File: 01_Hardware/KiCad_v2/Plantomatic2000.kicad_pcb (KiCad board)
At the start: 4 copper layers, 84 x 51 mm, 202 parts, among them J103 USB_C_Receptacle_USB2.0_16P, Q101 IRLL014NP, Q102 IRLL014NP, Q104 NVTA7002NT1G, Q105 RU1E002SPTCL, Q106 NVTA7002NT1G, Q107 NVTA7002NT1G, Q108 RU1E002SPTCL, Q109 NVTA7002NT1G, Q110 RU1E002SPTCL, Q111 DTC143Z, Q112 DTC143Z, Q113 CSD17313Q2, U101 XC6220B331MR, U102 nPM1300, U103 ESP32-WROOM-32E, U104 TPS61287, U105 USBLC6-2P6, U106 CP2102N-A02-GQFN24, U107 DS3231M, U108 AT24CS01-SSHM

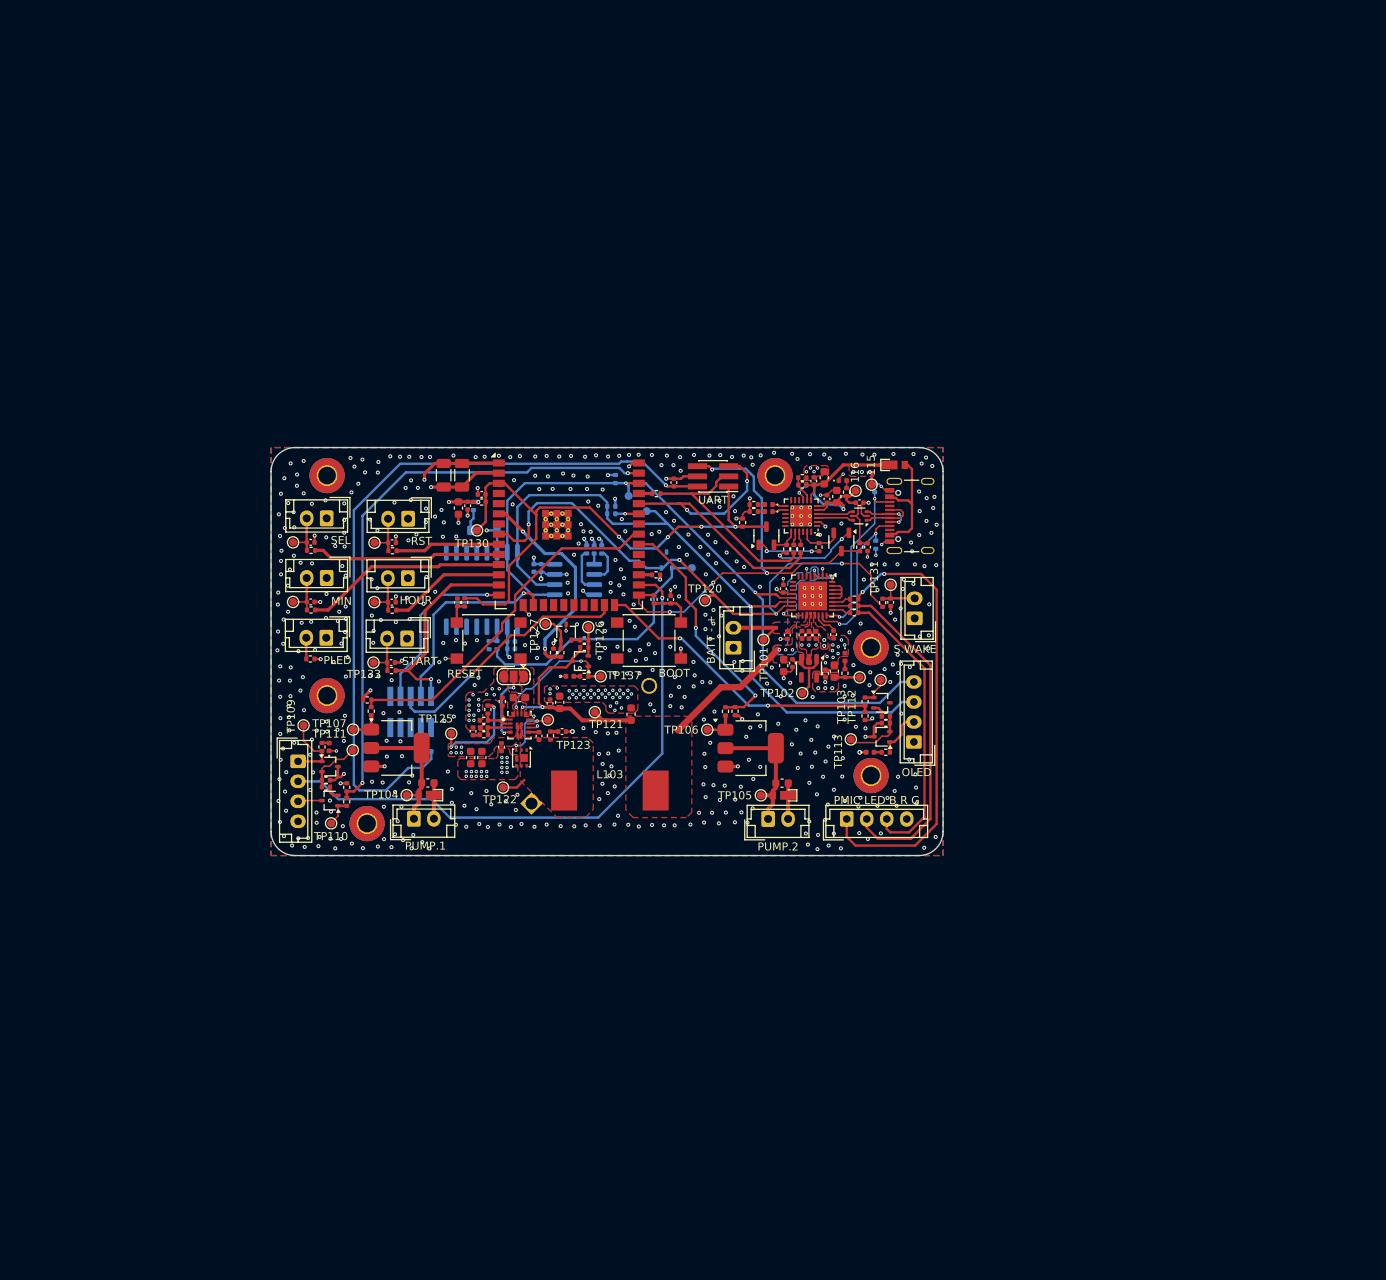
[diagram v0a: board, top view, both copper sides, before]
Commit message: Replaced BOOST converter, previous one didn't support +2A but rather 200 to 300mA, TO DO: re-do schematic annotation for BOOST, re-do BOM for BOOST
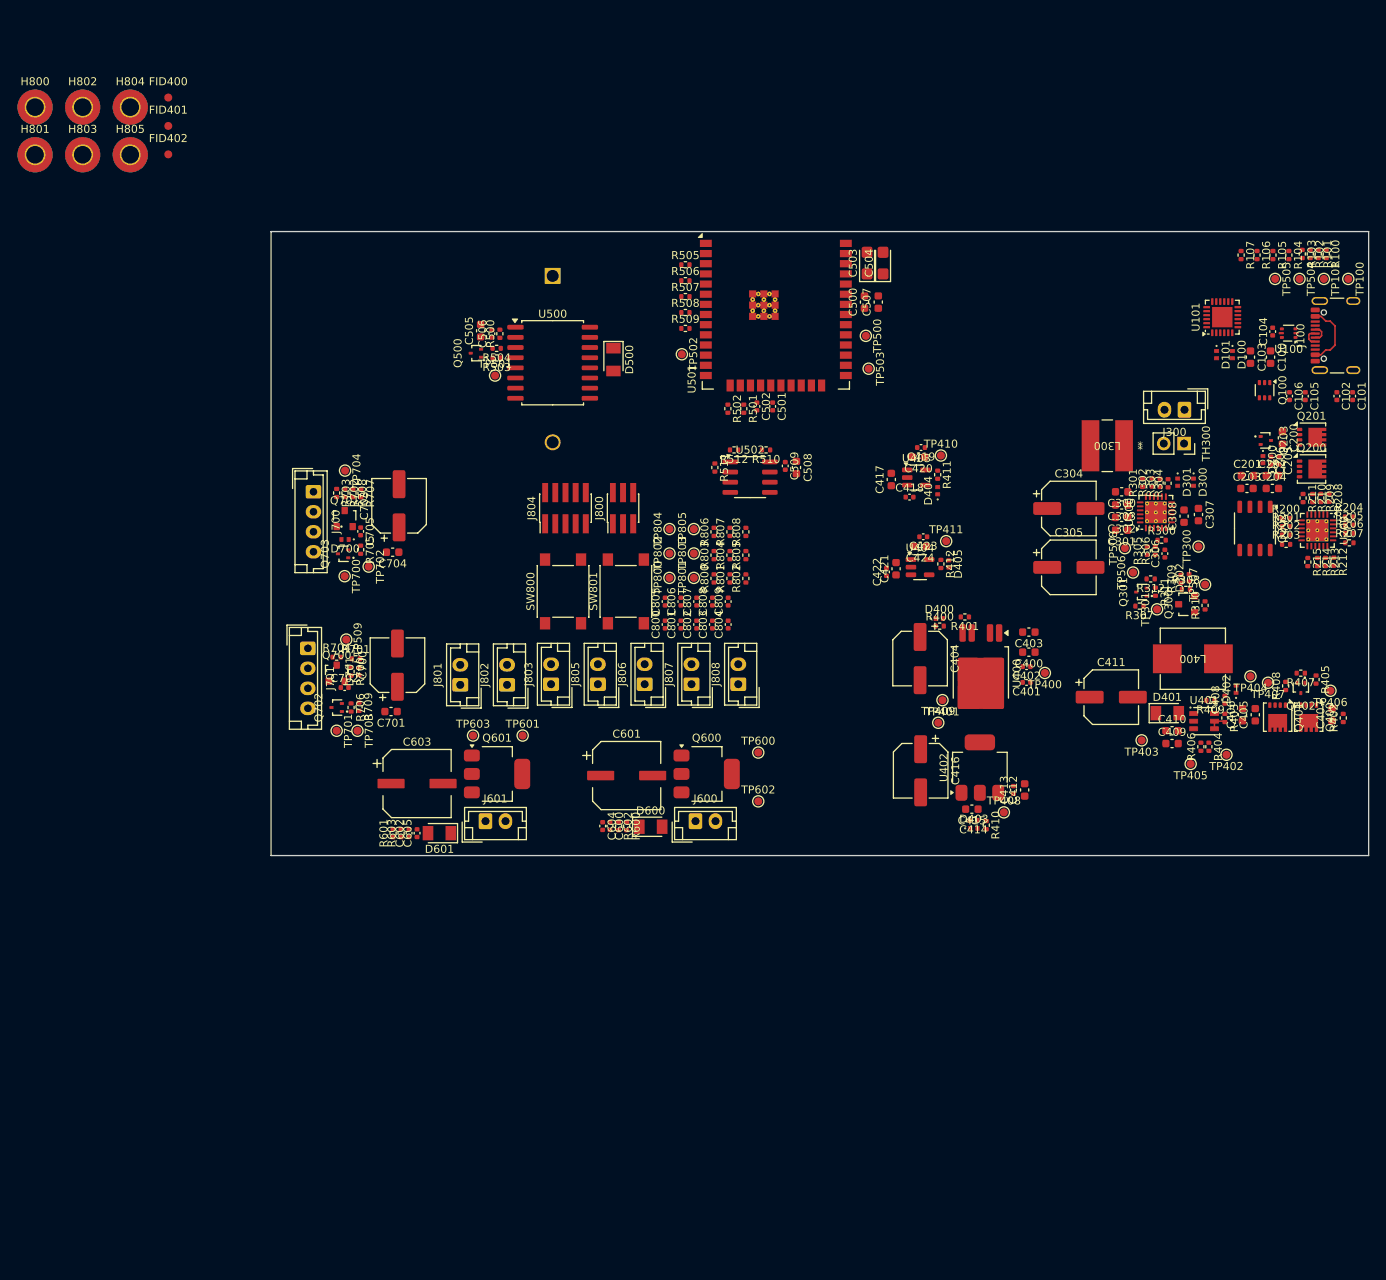
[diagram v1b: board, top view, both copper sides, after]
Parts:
- removed 115, 116, 132, 136, TP102, TP103, TP104, TP105, TP106, TP107, TP108, TP109, TP110, TP111, TP112, TP113, TP117, TP118, TP120, TP121, TP122, TP123, TP125, TP126, TP127, TP130, TP131, TP133, TP134, TP135, TP137: ~, TestPoint:TestPoint_Pad_D1.0mm
- removed BATT - +: Running LED, Connector_JST:JST_EH_B2B-EH-A_1x02_P2.50mm_Vertical
- removed BOOT, RESET: SW_Push, Button_Switch_SMD:SW_SPST_PTS645
- removed BT101: Battery_Cell, Battery:BatteryHolder_MYOUNG_BS-07-A1BJ001_CR2032
- removed C107, C108, C137, C144: 10uF, Capacitor_SMD:C_0402_1005Metric
- removed C109, C110, C123: 10uF, Capacitor_SMD:C_0603_1608Metric
- removed C111: 1uF, Capacitor_SMD:C_0402_1005Metric
- removed C112: 2.2uF, Capacitor_SMD:C_0402_1005Metric
- removed C113, C115, C116, C117, C118, C119, C122, C124, C129, C130, C132, C136, C138, C139, C140, C141, C142, C143, C145, C146, C147, C148: 100nF, Capacitor_SMD:C_0402_1005Metric
- removed C114, C133: 1uF, Capacitor_SMD:C_0603_1608Metric
- removed C120, C121: 47uF, Capacitor_SMD:C_0603_1608Metric
- removed C125: 58pF, Capacitor_SMD:C_0402_1005Metric
- removed C126, C135: 4.7nF, Capacitor_SMD:C_0402_1005Metric
- removed C127: 2.2uF, Capacitor_SMD:C_0603_1608Metric
- removed C128, C131: 4.7uF, Capacitor_SMD:C_0603_1608Metric
- removed C134: 22uF, Capacitor_SMD:C_0603_1608Metric
- removed D103, D104: SML-P13PTT86R, LED_SMD:LED_0402_1005Metric
- removed D106: 1N4148W, Diode_SMD:D_SOD-123
- removed D107, D111, D112, D113, D114: SML-P12U2TT86R, LED_SMD:LED_0402_1005Metric
- removed D108, D109, D110: SS14, Custom_Global_Footprints:SS14M_Flyback_Diode
- removed H101, H102, H103, H104, H105, H106: MountingHole_Pad, MountingHole:MountingHole_2.2mm_M2_Pad_TopBottom
- removed HOUR: Hour, Connector_JST:JST_EH_B2B-EH-A_1x02_P2.50mm_Vertical
- removed J103: USB_C_Receptacle_USB2.0_16P, Connector_USB:USB_C_Receptacle_Palconn_UTC16-G
- removed JTAG: Conn_02x05_Odd_Even, Connector_PinHeader_1.27mm:PinHeader_2x05_P1.27mm_Vertical_SMD
- removed L103: 4.7uH (SPM12565VT-4R7M-D), Custom_Global_Footprints:SPM12565VT-4R7M
- removed MIN: Minute, Connector_JST:JST_EH_B2B-EH-A_1x02_P2.50mm_Vertical
- removed OLED: JST_B4B, Connector_JST:JST_EH_B4B-EH-A_1x04_P2.50mm_Vertical
- removed PLED: Running LED, Connector_JST:JST_EH_B2B-EH-A_1x02_P2.50mm_Vertical
- removed PMIC LED B R G: JST_4B4, Connector_JST:JST_EH_B4B-EH-A_1x04_P2.50mm_Vertical
- removed PUMP.1, PUMP.2: JST_B2B, Connector_JST:JST_EH_B2B-EH-A_1x02_P2.50mm_Vertical
- removed Q101, Q102: IRLL014NP, Package_TO_SOT_SMD:SOT-223
- removed Q104, Q106, Q107, Q109: NVTA7002NT1G, Package_TO_SOT_SMD:SOT-323_SC-70
- removed Q105, Q108, Q110: RU1E002SPTCL, Package_TO_SOT_SMD:SOT-323_SC-70
- removed Q111, Q112: DTC143Z, Package_TO_SOT_SMD:SOT-23-3
- removed Q113: CSD17313Q2, Package_SON:Texas_DQK
- removed R108: 158K, Resistor_SMD:R_0402_1005Metric
- removed R109: 14K3, Resistor_SMD:R_0402_1005Metric
- removed R110, R121, R124, R126, R128, R129, R130, R132, R133, R140, R142, R143, R154: 10K, Resistor_SMD:R_0402_1005Metric
- removed R111: 40K, Resistor_SMD:R_0402_1005Metric
- removed R112, R119, R120, R123, R139, R148, R149, R150, R160, R161, R162, R163: 1K, Resistor_SMD:R_0402_1005Metric
- removed R113: 22K1, Resistor_SMD:R_0402_1005Metric
- removed R114, R115, R134, R135, R136, R137, R138, R146, R147, R164: 0R, Resistor_SMD:R_0402_1005Metric
- removed R116, R118, R159: 5K1, Resistor_SMD:R_0402_1005Metric
- removed R117: 47K5, Resistor_SMD:R_0402_1005Metric
- removed R122: 220R, Resistor_SMD:R_0402_1005Metric
- removed R125, R127, R131, R141, R156: 470R, Resistor_SMD:R_0402_1005Metric
- removed R144, R145, R151, R152, R153: 4K7, Resistor_SMD:R_0402_1005Metric
- removed R155, R157, R158: 12K, Resistor_SMD:R_0402_1005Metric
- removed RST: System Reset, Connector_JST:JST_EH_B2B-EH-A_1x02_P2.50mm_Vertical
- removed S.WAKE: System Wake Up, Connector_JST:JST_EH_B2B-EH-A_1x02_P2.50mm_Vertical
- removed SEL: ModSel, Jumper:SolderJumper-3_P1.3mm_Open_RoundedPad1.0x1.5mm
- removed SEL: Line Select, Connector_JST:JST_EH_B2B-EH-A_1x02_P2.50mm_Vertical
- removed START: Manual Start, Connector_JST:JST_EH_B2B-EH-A_1x02_P2.50mm_Vertical
- removed U102: nPM1300, Package_DFN_QFN:QFN-32-1EP_5x5mm_P0.5mm_EP3.6x3.6mm_ThermalVias
- removed U103: ESP32-WROOM-32E, RF_Module:ESP32-WROOM-32E
- removed U104: TPS61287, Custom_Global_Footprints:RZP0014A-MFG
- removed U105: USBLC6-2P6, Package_TO_SOT_SMD:SOT-666
- removed U106: CP2102N-A02-GQFN24, Package_DFN_QFN:QFN-24-1EP_4x4mm_P0.5mm_EP2.7x2.6mm_ThermalVias
- removed U107: DS3231M, Package_SO:SOIC-16W_7.5x10.3mm_P1.27mm
- removed U108: AT24CS01-SSHM, Package_SO:SOIC-8_3.9x4.9mm_P1.27mm
- removed UART: Conn_02x03_Odd_Even, Connector_PinHeader_1.27mm:PinHeader_2x03_P1.27mm_Vertical_SMD
- removed Water Sig: JST_4B4, Connector_JST:JST_EH_B4B-EH-A_1x04_P2.50mm_Vertical
- added BT500: BS-07-A1BJ001_CR2032, Battery:BatteryHolder_MYOUNG_BS-07-A1BJ001_CR2032, B.Cu at (149.8, 54.4)
- added C100: 4.7uF, Capacitor_SMD:C_0603_1608Metric, F.Cu at (239.5, 64.6)
- added C200: 4.7uF, Capacitor_SMD:C_0603_1608Metric, F.Cu at (241.0, 74.7)
- added C201: 1uF, Capacitor_SMD:C_0603_1608Metric, F.Cu at (236.7, 79.4)
- added C202: 1uF, Capacitor_SMD:C_0603_1608Metric, F.Cu at (239.8, 79.4)
- added C203: 1uF, Capacitor_SMD:C_0603_1608Metric, F.Cu at (236.6, 81.0)
- added C204: 1uF, Capacitor_SMD:C_0603_1608Metric, F.Cu at (239.8, 81.0)
- added C205: 100nF, Capacitor_SMD:C_0402_1005Metric, F.Cu at (240.6, 77.5)
- added C206: 100nF, Capacitor_SMD:C_0402_1005Metric, F.Cu at (239.6, 77.5)
- added C300: 1uF, Capacitor_SMD:C_0603_1608Metric, F.Cu at (220.9, 81.4)
- added C301: 10uF, Capacitor_SMD:C_0603_1608Metric, F.Cu at (220.9, 86.2)
- added C302: 10uF, Capacitor_SMD:C_0603_1608Metric, F.Cu at (220.9, 84.6)
- added C303: 10uF, Capacitor_SMD:C_0603_1608Metric, F.Cu at (220.9, 83.1)
- added C304: 47uF, Capacitor_SMD:CP_Elec_6.3x5.8, F.Cu at (214.3, 83.5)
- added C305: 47uF, Capacitor_SMD:CP_Elec_6.3x5.8, F.Cu at (214.3, 90.9)
- added C306: 47nF, Capacitor_SMD:C_0402_1005Metric, F.Cu at (226.3, 89.2)
- added C307: 10uF, Capacitor_SMD:C_0603_1608Metric, F.Cu at (230.5, 84.3)
- added C308: 4.7uF, Capacitor_SMD:C_0603_1608Metric, F.Cu at (228.7, 84.5)
- added C400: 10uF, Capacitor_SMD:C_0603_1608Metric, F.Cu at (209.3, 101.5)
- added C401: 100nF, Capacitor_SMD:C_0402_1005Metric, F.Cu at (209.0, 105.3)
- added C402: 100nF, Capacitor_SMD:C_0402_1005Metric, F.Cu at (209.0, 103.3)
- added C403: 10uF, Capacitor_SMD:C_0603_1608Metric, F.Cu at (209.3, 99.0)
- added C404: 47uF, Capacitor_SMD:CP_Elec_6.3x5.8, F.Cu at (195.7, 102.3)
- added C405: 1uF, Capacitor_SMD:C_0603_1608Metric, F.Cu at (237.6, 109.3)
- added C406: 1uF, Capacitor_SMD:C_0603_1608Metric, F.Cu at (236.0, 109.3)
- added C407: 1uF, Capacitor_SMD:C_0603_1608Metric, F.Cu at (247.2, 109.3)
- added C408: 100nF, Capacitor_SMD:C_0402_1005Metric, F.Cu at (233.8, 107.4)
- added C409: 1uF, Capacitor_SMD:C_0603_1608Metric, F.Cu at (227.2, 112.9)
- added C410: 10uF, Capacitor_SMD:C_0603_1608Metric, F.Cu at (227.2, 111.3)
- added C411: 47uF, Capacitor_SMD:CP_Elec_6.3x5.8, F.Cu at (219.6, 107.1)
- added C412: 10uF, Capacitor_SMD:C_0603_1608Metric, F.Cu at (208.8, 118.7)
- added C413: 100nF, Capacitor_SMD:C_0402_1005Metric, F.Cu at (207.4, 118.7)
- added C414: 100nF, Capacitor_SMD:C_0402_1005Metric, F.Cu at (202.4, 122.5)
- added C415: 10uF, Capacitor_SMD:C_0603_1608Metric, F.Cu at (202.2, 121.1)
- added C416: 47uF, Capacitor_SMD:CP_Elec_6.3x5.8, F.Cu at (195.8, 116.3)
- added C417: 10uF, Capacitor_SMD:C_0603_1608Metric, F.Cu at (192.1, 79.9)
- added C418: 100nF, Capacitor_SMD:C_0402_1005Metric, F.Cu at (194.4, 82.1)
- added C419: 100nF, Capacitor_SMD:C_0402_1005Metric, F.Cu at (195.8, 75.9)
- added C420: 10uF, Capacitor_SMD:C_0603_1608Metric, F.Cu at (195.5, 77.1)
- added C421: 10uF, Capacitor_SMD:C_0603_1608Metric, F.Cu at (192.7, 91.0)
- added C422: 100nF, Capacitor_SMD:C_0402_1005Metric, F.Cu at (191.5, 91.5)
- added C423: 100nF, Capacitor_SMD:C_0402_1005Metric, F.Cu at (196.1, 87.0)
- added C424: 10uF, Capacitor_SMD:C_0603_1608Metric, F.Cu at (195.7, 88.2)
- added C500: 22uF, Capacitor_SMD:C_0603_1608Metric, F.Cu at (188.8, 57.7)
- added C501: 100nF, Capacitor_SMD:C_0402_1005Metric, F.Cu at (177.3, 70.8)
- added C502: 100nF, Capacitor_SMD:C_0402_1005Metric, F.Cu at (175.3, 70.8)
- added C503: 10uF, Capacitor_Tantalum_SMD:CP_EIA-3216-18_Kemet-A, F.Cu at (189.1, 52.8)
- added C504: 10uF, Capacitor_Tantalum_SMD:CP_EIA-3216-18_Kemet-A, F.Cu at (191.1, 52.8)
- added C505: 10uF, Capacitor_SMD:C_0603_1608Metric, F.Cu at (140.8, 61.3)
- added C506: 100nF, Capacitor_SMD:C_0402_1005Metric, F.Cu at (142.2, 61.7)
- added C507: 1uF, Capacitor_SMD:C_0603_1608Metric, F.Cu at (190.5, 57.7)
- added C508: 10uF, Capacitor_SMD:C_0603_1608Metric, F.Cu at (180.3, 78.4)
- added C509: 100nF, Capacitor_SMD:C_0402_1005Metric, F.Cu at (178.9, 78.2)
- added C600: 100nF, Capacitor_SMD:C_0402_1005Metric, F.Cu at (157.0, 123.2)
- added C601: 220uF, Custom_Global_Footprints:EEEFK1V470P, F.Cu at (159.1, 116.9)
- added C602: 100nF, Capacitor_SMD:C_0402_1005Metric, F.Cu at (131.8, 124.1)
- added C603: 220uF, Custom_Global_Footprints:EEEFK1V470P, F.Cu at (132.8, 117.9)
- added C604: 100nF, Capacitor_SMD:C_0402_1005Metric, F.Cu at (156.1, 123.2)
- added C605: 100nF, Capacitor_SMD:C_0402_1005Metric, F.Cu at (132.8, 124.1)
- added C700: 47uF, Capacitor_SMD:CP_Elec_6.3x5.8, F.Cu at (130.4, 103.1)
- added C701: 10uF, Capacitor_SMD:C_0603_1608Metric, F.Cu at (129.6, 108.9)
- added C702: 100nF, Capacitor_SMD:C_0402_1005Metric, F.Cu at (123.8, 105.9)
- added C703: 47uF, Capacitor_SMD:CP_Elec_6.3x5.8, F.Cu at (130.6, 83.2)
- added C704: 10uF, Capacitor_SMD:C_0603_1608Metric, F.Cu at (129.8, 89.0)
- added C705: 100nF, Capacitor_SMD:C_0402_1005Metric, F.Cu at (125.8, 86.4)
- added C800: 100nF, Capacitor_SMD:C_0402_1005Metric, F.Cu at (163.9, 98.0)
- added C801: 100nF, Capacitor_SMD:C_0402_1005Metric, F.Cu at (165.8, 98.0)
- added C802: 100nF, Capacitor_SMD:C_0402_1005Metric, F.Cu at (167.8, 98.0)
- added C803: 100nF, Capacitor_SMD:C_0402_1005Metric, F.Cu at (169.8, 98.0)
- added C804: 100nF, Capacitor_SMD:C_0402_1005Metric, F.Cu at (171.7, 98.0)
- added C805: 100nF, Capacitor_SMD:C_0402_1005Metric, F.Cu at (163.9, 95.2)
- added C806: 100nF, Capacitor_SMD:C_0402_1005Metric, F.Cu at (165.8, 95.2)
- added C807: 100nF, Capacitor_SMD:C_0402_1005Metric, F.Cu at (167.8, 95.2)
- added C808: 100nF, Capacitor_SMD:C_0402_1005Metric, F.Cu at (169.8, 95.2)
- added C809: 100nF, Capacitor_SMD:C_0402_1005Metric, F.Cu at (171.7, 95.2)
- added D100: NCD0402G1, Custom_Global_Footprints:SML-P13PTT_LED_0402_1005Metric, F.Cu at (234.8, 64.3)
- added D101: NCD0402G1, Custom_Global_Footprints:SML-P13PTT_LED_0402_1005Metric, F.Cu at (232.8, 64.3)
- added D200: NCD0402R1, Custom_Global_Footprints:SML-P13PTT_LED_0402_1005Metric, F.Cu at (238.6, 77.4)
- added D300: NCD0402G1, Custom_Global_Footprints:SML-P13PTT_LED_0402_1005Metric, F.Cu at (229.9, 80.2)
- added D301: NCD0402R1, Custom_Global_Footprints:SML-P13PTT_LED_0402_1005Metric, F.Cu at (227.9, 80.2)
- added D302: NCD0402G1, Custom_Global_Footprints:SML-P13PTT_LED_0402_1005Metric, F.Cu at (229.3, 92.2)
- added D400: NCD0402R1, Custom_Global_Footprints:SML-P13PTT_LED_0402_1005Metric, F.Cu at (198.1, 97.3)
- added D401: SBR3U40S1F, Custom_Global_Footprints:SBR3U40S1F-7, F.Cu at (226.6, 109.1)
- added D402: NCD0402G1, Custom_Global_Footprints:SML-P13PTT_LED_0402_1005Metric, F.Cu at (235.2, 106.1)
- added D403: NCD0402R1, Custom_Global_Footprints:SML-P13PTT_LED_0402_1005Metric, F.Cu at (202.4, 123.5)
- added D404: NCD0402R1, Custom_Global_Footprints:SML-P13PTT_LED_0402_1005Metric, F.Cu at (197.9, 81.3)
- added D405: NCD0402R1, Custom_Global_Footprints:SML-P13PTT_LED_0402_1005Metric, F.Cu at (199.3, 90.5)
- added D500: SBR3U40S1F, Custom_Global_Footprints:SBR3U40S1F-7, F.Cu at (157.4, 64.9)
- added D600: SBR3U40S1F, Custom_Global_Footprints:SBR3U40S1F-7, F.Cu at (162.1, 123.3)
- added D601: SBR3U40S1F, Custom_Global_Footprints:SBR3U40S1F-7, F.Cu at (135.7, 124.1)
- added D700: NCD0402R1, Custom_Global_Footprints:SML-P13PTT_LED_0402_1005Metric, F.Cu at (123.8, 87.4)
- added D701: NCD0402R1, Custom_Global_Footprints:SML-P13PTT_LED_0402_1005Metric, F.Cu at (125.6, 103.9)
- added FID400: Fiducial, Fiducial:Fiducial_1mm_Mask2mm, F.Cu at (101.8, 32.1)
- added FID401: Fiducial, Fiducial:Fiducial_1mm_Mask2mm, F.Cu at (101.8, 35.7)
- added FID402: Fiducial, Fiducial:Fiducial_1mm_Mask2mm, F.Cu at (101.8, 39.2)
- added H800: MountingHole_Pad, MountingHole:MountingHole_2.2mm_M2_Pad_TopBottom, F.Cu at (85.1, 33.4)
- added H801: MountingHole_Pad, MountingHole:MountingHole_2.2mm_M2_Pad_TopBottom, F.Cu at (85.1, 39.3)
- added H802: MountingHole_Pad, MountingHole:MountingHole_2.2mm_M2_Pad_TopBottom, F.Cu at (91.0, 33.4)
- added H803: MountingHole_Pad, MountingHole:MountingHole_2.2mm_M2_Pad_TopBottom, F.Cu at (91.0, 39.3)
- added H804: MountingHole_Pad, MountingHole:MountingHole_2.2mm_M2_Pad_TopBottom, F.Cu at (97.0, 33.4)
- added H805: MountingHole_Pad, MountingHole:MountingHole_2.2mm_M2_Pad_TopBottom, F.Cu at (97.0, 39.3)
- added J100: TYPE-C-31-M-12, Connector_USB:USB_C_Receptacle_GCT_USB4105-xx-A_16P_TopMnt_Horizontal, F.Cu at (248.8, 61.9)
- added J300: JST_B2B, Connector_JST:JST_EH_B2B-EH-A_1x02_P2.50mm_Vertical, F.Cu at (228.8, 71.2)
- added J600: JST_B2B, Connector_JST:JST_EH_B2B-EH-A_1x02_P2.50mm_Vertical, F.Cu at (167.7, 122.6)
- added J601: JST_B2B, Connector_JST:JST_EH_B2B-EH-A_1x02_P2.50mm_Vertical, F.Cu at (141.4, 122.6)
- added J700: JST_B4B, Connector_JST:JST_EH_B4B-EH-A_1x04_P2.50mm_Vertical, F.Cu at (119.9, 81.4)
- added J701: JST_B4B, Connector_JST:JST_EH_B4B-EH-A_1x04_P2.50mm_Vertical, F.Cu at (119.2, 101.0)
- added J800: Conn_02x03_Odd_Even, Connector_PinHeader_1.27mm:PinHeader_2x03_P1.27mm_Vertical_SMD, F.Cu at (158.6, 83.5)
- added J801: JST_B2B, Connector_JST:JST_EH_B2B-EH-A_1x02_P2.50mm_Vertical, F.Cu at (138.2, 105.6)
- added J802: JST_B2B, Connector_JST:JST_EH_B2B-EH-A_1x02_P2.50mm_Vertical, F.Cu at (144.1, 105.6)
- added J803: JST_B2B, Connector_JST:JST_EH_B2B-EH-A_1x02_P2.50mm_Vertical, F.Cu at (149.6, 105.5)
- added J804: Conn_02x05_Odd_Even, Connector_PinHeader_1.27mm:PinHeader_2x05_P1.27mm_Vertical_SMD, F.Cu at (151.4, 83.5)
- added J805: JST_B2B, Connector_JST:JST_EH_B2B-EH-A_1x02_P2.50mm_Vertical, F.Cu at (155.4, 105.5)
- added J806: JST_B2B, Connector_JST:JST_EH_B2B-EH-A_1x02_P2.50mm_Vertical, F.Cu at (161.3, 105.5)
- added J807: JST_B2B, Connector_JST:JST_EH_B2B-EH-A_1x02_P2.50mm_Vertical, F.Cu at (167.2, 105.5)
- added J808: JST_B2B, Connector_JST:JST_EH_B2B-EH-A_1x02_P2.50mm_Vertical, F.Cu at (173.0, 105.5)
- added L300: SRN6045HA-1R0Y, Custom_Global_Footprints:SRN6045HA-1R0Y, F.Cu at (219.1, 75.7)
- added L400: ETQ-P5M100YFM, Custom_Global_Footprints:ETQ-P5M100YFM, F.Cu at (229.8, 102.3)
- added Q100: UMH3N, Package_TO_SOT_SMD:SOT-363_SC-70-6, F.Cu at (238.8, 68.7)
- added Q200: SI7615DN-T1-GE3, Package_SON:Diodes_PowerDI3333-8, F.Cu at (244.7, 78.6)
- added Q201: SI7615DN-T1-GE3, Package_SON:Diodes_PowerDI3333-8, F.Cu at (244.7, 74.6)
- added Q202: DMP6050SSD, Custom_Global_Footprints:DMP6050SSD_SO-8_3.9x4.9mm_P1.27mm, F.Cu at (237.6, 86.0)
- added Q203: NVTA7002NT1G, Custom_Global_Footprints:NVTA7002N, F.Cu at (238.9, 75.0)
- added Q300: BSS314PE, Custom_Global_Footprints:BSS314PE, F.Cu at (229.1, 95.5)
- added Q301: NVTA7002NT1G, Custom_Global_Footprints:NVTA7002N, F.Cu at (223.4, 94.0)
- added Q400: SI7615DN-T1-GE3, Package_SON:Diodes_PowerDI3333-8, F.Cu at (244.3, 109.6)
- added Q401: SI7615DN-T1-GE3, Package_SON:Diodes_PowerDI3333-8, F.Cu at (240.4, 109.6)
- added Q402: NVTA7002NT1G, Custom_Global_Footprints:NVTA7002N, F.Cu at (243.3, 105.9)
- added Q500: NVTA7002NT1G, Custom_Global_Footprints:NVTA7002N, F.Cu at (140.2, 64.1)
- added Q600: STN3NF06L, Package_TO_SOT_SMD:SOT-223, F.Cu at (169.1, 116.7)
- added Q601: STN3NF06L, Package_TO_SOT_SMD:SOT-223, F.Cu at (142.8, 116.7)
- added Q700: BSS314PE, Custom_Global_Footprints:BSS314PE, F.Cu at (122.8, 104.1)
- added Q701: BSS314PE, Custom_Global_Footprints:BSS314PE, F.Cu at (123.8, 84.8)
- added Q702: NVTA7002NT1G, Custom_Global_Footprints:NVTA7002N, F.Cu at (122.8, 108.4)
- added Q703: NVTA7002NT1G, Custom_Global_Footprints:NVTA7002N, F.Cu at (123.6, 89.2)
- added R100: 22K1, Resistor_SMD:R_0402_1005Metric, F.Cu at (246.5, 51.7)
- added R101: 1K, Resistor_SMD:R_0402_1005Metric, F.Cu at (245.5, 51.7)
- added R200: 10K, Resistor_SMD:R_0402_1005Metric, F.Cu at (241.4, 84.8)
- added R201: 49K9, Resistor_SMD:R_0402_1005Metric, F.Cu at (241.5, 85.8)
- added R202: 1K, Resistor_SMD:R_0402_1005Metric, F.Cu at (241.5, 86.8)
- added R203: 1K, Resistor_SMD:R_0402_1005Metric, F.Cu at (241.5, 88.0)
- added R204: 1K, Resistor_SMD:R_0402_1005Metric, F.Cu at (249.3, 84.6)
- added R205: 470R, Resistor_SMD:R_0402_1005Metric, F.Cu at (249.4, 85.6)
- added R206: 4K7, Resistor_SMD:R_0402_1005Metric, F.Cu at (249.4, 86.6)
- added R207: 10K, Resistor_SMD:R_0402_1005Metric, F.Cu at (249.4, 87.8)
- added R208: 10K, Resistor_SMD:R_0402_1005Metric, F.Cu at (246.8, 82.2)
- added R209: 10K, Resistor_SMD:R_0402_1005Metric, F.Cu at (245.8, 82.2)
- added R210: 0R, Resistor_SMD:R_0402_1005Metric, F.Cu at (244.8, 82.2)
- added R211: 10K, Resistor_SMD:R_0402_1005Metric, F.Cu at (243.6, 82.2)
- added R212: 0R, Resistor_SMD:R_0402_1005Metric, F.Cu at (247.4, 90.2)
- added R213: 0R, Resistor_SMD:R_0402_1005Metric, F.Cu at (246.4, 90.2)
- added R214: 10K, Resistor_SMD:R_0402_1005Metric, F.Cu at (245.4, 90.2)
- added R215: 0R, Resistor_SMD:R_0402_1005Metric, F.Cu at (244.2, 90.2)
- added R300: 1K, Resistor_SMD:R_0402_1005Metric, F.Cu at (225.9, 87.5)
- added R301: 1K, Resistor_SMD:R_0402_1005Metric, F.Cu at (223.5, 80.3)
- added R302: 10K, Resistor_SMD:R_0402_1005Metric, F.Cu at (224.7, 80.3)
- added R303: 10K, Resistor_SMD:R_0402_1005Metric, F.Cu at (225.7, 80.3)
- added R304: 5K23, Resistor_SMD:R_0402_1005Metric, F.Cu at (226.7, 80.4)
- added R305: 130R, Resistor_SMD:R_0402_1005Metric, F.Cu at (224.1, 88.8)
- added R306: 30K1, Resistor_SMD:R_0402_1005Metric, F.Cu at (225.1, 88.8)
- added R307: 10K, Resistor_SMD:R_0402_1005Metric, F.Cu at (223.2, 95.7)
- added R308: 22K1, Resistor_SMD:R_0402_1005Metric, F.Cu at (228.9, 93.6)
- added R309: 1K, Resistor_SMD:R_0402_1005Metric, F.Cu at (228.3, 92.3)
- added R310: 10K, Resistor_SMD:R_0402_1005Metric, F.Cu at (231.3, 95.6)
- added R311: 470R, Resistor_SMD:R_0402_1005Metric, F.Cu at (225.2, 93.9)
- added R312: 10K, Resistor_SMD:R_0402_1005Metric, F.Cu at (224.6, 92.3)
- added R400: 4K7, Resistor_SMD:R_0402_1005Metric, F.Cu at (198.2, 98.2)
- added R401: 10K, Resistor_SMD:R_0402_1005Metric, F.Cu at (201.3, 97.1)
- added R402: 10K, Resistor_SMD:R_0402_1005Metric, F.Cu at (248.6, 109.7)
- added R403: 10K, Resistor_SMD:R_0402_1005Metric, F.Cu at (233.8, 109.7)
- added R404: 1M, Resistor_SMD:R_0402_1005Metric, F.Cu at (231.8, 113.3)
- added R405: 470R, Resistor_SMD:R_0402_1005Metric, F.Cu at (245.2, 104.9)
- added R406: 64K9, Resistor_SMD:R_0402_1005Metric, F.Cu at (230.8, 113.3)
- added R407: 10K, Resistor_SMD:R_0402_1005Metric, F.Cu at (243.3, 104.1)
- added R408: 22K1, Resistor_SMD:R_0402_1005Metric, F.Cu at (241.4, 105.7)
- added R409: 1K, Resistor_SMD:R_0402_1005Metric, F.Cu at (232.0, 107.5)
- added R410: 4K7, Resistor_SMD:R_0402_1005Metric, F.Cu at (204.0, 123.1)
- added R411: 1K, Resistor_SMD:R_0402_1005Metric, F.Cu at (197.9, 79.3)
- added R412: 1K, Resistor_SMD:R_0402_1005Metric, F.Cu at (198.3, 90.5)
- added R500: 220R, Resistor_SMD:R_0402_1005Metric, F.Cu at (143.2, 61.7)
- added R501: 10K, Resistor_SMD:R_0402_1005Metric, F.Cu at (173.7, 71.0)
- added R502: 0R, Resistor_SMD:R_0402_1005Metric, F.Cu at (171.7, 71.0)
- added R503: 470R, Resistor_SMD:R_0402_1005Metric, F.Cu at (142.8, 64.7)
- added R504: 10K, Resistor_SMD:R_0402_1005Metric, F.Cu at (142.8, 63.5)
- added R505: 10K, Resistor_SMD:R_0402_1005Metric, F.Cu at (166.4, 53.0)
- added R506: 4K7, Resistor_SMD:R_0402_1005Metric, F.Cu at (166.4, 55.0)
- added R507: 4K7, Resistor_SMD:R_0402_1005Metric, F.Cu at (166.4, 57.0)
- added R508: 0R, Resistor_SMD:R_0402_1005Metric, F.Cu at (166.4, 59.0)
- added R509: 0R, Resistor_SMD:R_0402_1005Metric, F.Cu at (166.4, 61.0)
- added R510: 4K7, Resistor_SMD:R_0402_1005Metric, F.Cu at (176.5, 76.2)
- added R511: 4K7, Resistor_SMD:R_0402_1005Metric, F.Cu at (170.1, 78.4)
- added R512: 4K7, Resistor_SMD:R_0402_1005Metric, F.Cu at (172.5, 76.2)
- added R600: 470R, Resistor_SMD:R_0402_1005Metric, F.Cu at (159.1, 123.2)
- added R601: 470R, Resistor_SMD:R_0402_1005Metric, F.Cu at (129.8, 124.1)
- added R602: 10K, Resistor_SMD:R_0402_1005Metric, F.Cu at (158.1, 123.2)
- added R603: 10K, Resistor_SMD:R_0402_1005Metric, F.Cu at (130.8, 124.1)
- added R700: 22K1, Resistor_SMD:R_0402_1005Metric, F.Cu at (124.6, 103.9)
- added R701: 1K, Resistor_SMD:R_0402_1005Metric, F.Cu at (125.2, 102.3)
- added R702: 22K1, Resistor_SMD:R_0402_1005Metric, F.Cu at (123.8, 81.6)
- added R703: 4K7, Resistor_SMD:R_0402_1005Metric, F.Cu at (122.8, 81.6)
- added R704: 10K, Resistor_SMD:R_0402_1005Metric, F.Cu at (122.8, 102.1)
- added R705: 10K, Resistor_SMD:R_0402_1005Metric, F.Cu at (125.8, 88.7)
- added R706: 470R, Resistor_SMD:R_0402_1005Metric, F.Cu at (124.6, 108.4)
- added R707: 470R, Resistor_SMD:R_0402_1005Metric, F.Cu at (125.8, 81.6)
- added R708: 10K, Resistor_SMD:R_0402_1005Metric, F.Cu at (124.8, 81.6)
- added R709: 10K, Resistor_SMD:R_0402_1005Metric, F.Cu at (125.6, 108.3)
- added R800: 0R, Resistor_SMD:R_0402_1005Metric, F.Cu at (170.0, 92.3)
- added R801: 0R, Resistor_SMD:R_0402_1005Metric, F.Cu at (172.0, 92.3)
- added R802: 0R, Resistor_SMD:R_0402_1005Metric, F.Cu at (173.9, 92.3)
- added R803: 0R, Resistor_SMD:R_0402_1005Metric, F.Cu at (170.0, 89.3)
- added R804: 0R, Resistor_SMD:R_0402_1005Metric, F.Cu at (172.0, 89.3)
- added R805: 0R, Resistor_SMD:R_0402_1005Metric, F.Cu at (173.9, 89.3)
- added R806: 0R, Resistor_SMD:R_0402_1005Metric, F.Cu at (170.0, 86.4)
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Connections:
- C101 pad 1: Net-(U102-VBUSOUT) -> +VBUS
- C102 pad 1: +3V3 -> +VDD
- C103 pad 1: +3V3 -> +VDD
- C104 pad 1: +3V3 -> +VBUS
- C105 pad 1: +3V3 -> Net-(J100-SHIELD)
- C106 pad 1: VBUS -> Net-(J100-SHIELD)
- R102 pad 1: PUMP1_EN -> ESP_RX
- R102 pad 2: Net-(Q101-G) -> /USB_C_TO_SERIAL/SER_TX
- R103 pad 1: GND -> /USB_C_TO_SERIAL/VBUS_VDIV
- R103 pad 2: PUMP1_EN -> GND
- R104 pad 1: Net-(U103-IO16) -> ESP_TX
- R104 pad 2: +3V3 -> /USB_C_TO_SERIAL/SER_RX
- R105 pad 1: PUMP2_EN -> +VDD
- R106 pad 1: GND -> +VDD
- R106 pad 2: PUMP2_EN -> Net-(D101-A)
- R107 pad 1: /ESP_EN -> Net-(J100-SHIELD)
- R107 pad 2: Net-(C118-Pad1) -> GND
- TP101 pad 1: +VBAT -> +VBUS
- U101 pad 1: +VSYS -> unconnected-(U101-~{RI}/CLK-Pad1)
- U101 pad 3: +VSYS -> /USB_C_TO_SERIAL/USB_D+
- U101 pad 4: unconnected-(U101-NC-Pad4) -> /USB_C_TO_SERIAL/USB_D-
- U101 pad 5: +3V3 -> +VDD
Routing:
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- removed copper zone on F.Cu, net +12V
- removed copper zone on In1.Cu, net +12V
- removed copper zone on F.Cu, net +3V3
- removed copper zone on In1.Cu, net +3V3
- removed copper zone on F.Cu, net +VBAT
- removed copper zone on B.Cu, net +VSYS
- removed copper zone on F.Cu, net +VSYS
- removed copper zone on F.Cu, net /CVCC
- removed copper zone on F.Cu, net /SW
- removed copper zone on B.Cu, net GND
- removed copper zone on F.Cu, net GND
- removed copper zone on In1.Cu, net GND
- removed copper zone on In2.Cu, net GND
- removed copper zone on F.Cu, net VBUS
- removed copper zone on In1.Cu, net VBUS
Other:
- board size 84 x 51 mm -> 137.2 x 78 mm

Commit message: USB-C and Serial PCB routing done
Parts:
- removed C304, C305, C411, C416, C700, C703: 47uF, Capacitor_SMD:CP_Elec_6.3x5.8
- removed C407, C409: 1uF, Capacitor_SMD:C_0603_1608Metric
- removed C408: 100nF, Capacitor_SMD:C_0402_1005Metric
- removed C410: 10uF, Capacitor_SMD:C_0603_1608Metric
- removed D401: SBR3U40S1F, Custom_Global_Footprints:SBR3U40S1F-7
- removed D402: NCD0402G1, Custom_Global_Footprints:SML-P13PTT_LED_0402_1005Metric
- removed L400: ETQ-P5M100YFM, Custom_Global_Footprints:ETQ-P5M100YFM
- removed Q400, Q401: SI7615DN-T1-GE3, Package_SON:Diodes_PowerDI3333-8
- removed Q402: NVTA7002NT1G, Custom_Global_Footprints:NVTA7002N
- removed R200, R401, R402, R403, R407: 10K, Resistor_SMD:R_0402_1005Metric
- removed R404: 1M, Resistor_SMD:R_0402_1005Metric
- removed R406: 64K9, Resistor_SMD:R_0402_1005Metric
- removed R408: 22K1, Resistor_SMD:R_0402_1005Metric
- removed R409: 1K, Resistor_SMD:R_0402_1005Metric
- removed TP100, TP101, TP404, TP406, TP407, TP410, TP411, TP504, TP505, TP508: ~, TestPoint:TestPoint_Pad_D1.0mm
- removed TP300: +VBAT, TestPoint:TestPoint_Pad_D1.0mm
- removed TP400, TP401, TP408, TP409: TestPoint_Small, TestPoint:TestPoint_Pad_D1.0mm
- removed U400: BDJ2FC0WFP, Package_TO_SOT_SMD:TO-252-4
- removed U401: TLV61048, Custom_Global_Footprints:TLV61048
- removed U402: NCP1117-12_SOT223, Package_TO_SOT_SMD:SOT-223
- added C122: 100nF, Capacitor_SMD:C_0402_1005Metric, F.Cu at (193.6, 46.5)
- added C123: 10uF, Capacitor_SMD:C_0603_1608Metric, F.Cu at (191.1, 36.8)
- added C124: 100nF, Capacitor_SMD:C_0402_1005Metric, F.Cu at (193.6, 48.5)
- added C125: 100pF, Capacitor_SMD:C_0402_1005Metric, F.Cu at (193.6, 50.5)
- added C126: 22nF, Capacitor_SMD:C_0402_1005Metric, F.Cu at (193.6, 52.4)
- added C127: 4.7uF, Capacitor_SMD:C_0603_1608Metric, F.Cu at (191.1, 39.3)
- added C128: 47uF, Capacitor_SMD:C_1206_3216Metric, F.Cu at (223.4, 80.8)
- added C129: 47uF, Capacitor_SMD:C_1206_3216Metric, F.Cu at (223.4, 84.1)
- added C130: 47uF, Capacitor_SMD:C_1206_3216Metric, F.Cu at (206.2, 25.1)
- added C131: 47uF, Capacitor_SMD:C_1206_3216Metric, F.Cu at (206.2, 28.5)
- added C132: 47uF, Capacitor_SMD:C_1206_3216Metric, F.Cu at (179.1, 123.3)
- added C133: 47uF, Capacitor_SMD:C_1206_3216Metric, F.Cu at (179.1, 126.6)
- added C135: 22nF, Capacitor_SMD:C_0402_1005Metric, F.Cu at (193.6, 54.4)
- added C207: 1uF, Capacitor_SMD:C_0603_1608Metric, F.Cu at (191.1, 41.8)
- added C208: 1uF, Capacitor_SMD:C_0603_1608Metric, F.Cu at (191.1, 44.3)
- added C510: 22uF, Capacitor_SMD:C_0805_2012Metric, F.Cu at (191.3, 25.0)
- added C511: 22uF, Capacitor_SMD:C_0805_2012Metric, F.Cu at (191.3, 28.0)
- added C512: 22uF, Capacitor_SMD:C_0805_2012Metric, F.Cu at (191.3, 31.0)
- added C513: 22uF, Capacitor_SMD:C_0805_2012Metric, F.Cu at (191.3, 34.0)
- added D201: NCD0402R1, LED_SMD:LED_0402_1005Metric, F.Cu at (190.7, 46.5)
- added L103: 4.7uH (SPM12565VT-4R7M-D), Custom_Global_Footprints:SPM12565VT-4R7M, F.Cu at (179.2, 54.7)
- added Q113: CSD17313Q2, Package_SON:Texas_DQK, F.Cu at (173.3, 63.1)
- added Q204: SI7615DN-T1-GE3, Package_SON:Diodes_PowerDI3333-8, F.Cu at (206.2, 32.7)
- added Q205: IRLML2402TRPBF, Package_TO_SOT_SMD:SOT-23, F.Cu at (208.1, 62.6)
- added R108: 158K, Resistor_SMD:R_0402_1005Metric, F.Cu at (202.5, 36.5)
- added R109: 14K3, Resistor_SMD:R_0402_1005Metric, F.Cu at (202.5, 38.5)
- added R110: 49K9, Resistor_SMD:R_0402_1005Metric, F.Cu at (202.5, 40.5)
- added R111: 20K, Resistor_SMD:R_0402_1005Metric, F.Cu at (202.5, 42.5)
- added R112: 22K1, Resistor_SMD:R_0402_1005Metric, F.Cu at (202.5, 44.5)
- added R121: 10K, Resistor_SMD:R_0402_1005Metric, F.Cu at (205.4, 36.5)
- added R216: 49K9, Resistor_SMD:R_0402_1005Metric, F.Cu at (132.6, 159.4)
- added R217: 49K9, Resistor_SMD:R_0402_1005Metric, F.Cu at (205.4, 38.5)
- added R218: 1K, Resistor_SMD:R_0402_1005Metric, F.Cu at (205.4, 40.5)
- added TP412: TestPoint_Small, TestPoint:TestPoint_Pad_D1.5mm, F.Cu at (152.1, 105.8)
- added TP413: TestPoint_Small, TestPoint:TestPoint_Pad_D1.5mm, F.Cu at (113.0, 144.4)
- added TP414: TestPoint_Small, TestPoint:TestPoint_Pad_D1.5mm, F.Cu at (113.0, 147.9)
- added TP415: TestPoint_Small, TestPoint:TestPoint_Pad_D1.5mm, F.Cu at (113.0, 151.5)
- added TP416: TestPoint_Small, TestPoint:TestPoint_Pad_D1.5mm, F.Cu at (113.0, 155.0)
- added TP417: TestPoint_Small, TestPoint:TestPoint_Pad_D1.5mm, F.Cu at (116.6, 144.4)
- added TP418: TestPoint_Small, TestPoint:TestPoint_Pad_D1.5mm, F.Cu at (116.6, 147.9)
- added TP419: TestPoint_Small, TestPoint:TestPoint_Pad_D1.5mm, F.Cu at (116.6, 151.5)
- added TP420: TestPoint_Small, TestPoint:TestPoint_Pad_D1.5mm, F.Cu at (218.8, 74.6)
- added TP421: TestPoint_Small, TestPoint:TestPoint_Pad_D1.5mm, F.Cu at (218.8, 78.1)
- added TP422: TestPoint_Small, TestPoint:TestPoint_Pad_D1.5mm, F.Cu at (218.8, 81.7)
- added TP423: TestPoint_Small, TestPoint:TestPoint_Pad_D1.5mm, F.Cu at (218.8, 85.2)
- added TP424: TestPoint_Small, TestPoint:TestPoint_Pad_D1.5mm, F.Cu at (202.6, 54.9)
- added TP425: TestPoint_Small, TestPoint:TestPoint_Pad_D1.5mm, F.Cu at (202.6, 58.4)
- added TP426: TestPoint_Small, TestPoint:TestPoint_Pad_D1.5mm, F.Cu at (206.1, 54.9)
- added TP427: TestPoint_Small, TestPoint:TestPoint_Pad_D1.5mm, F.Cu at (206.1, 58.4)
- added TP428: TestPoint_Small, TestPoint:TestPoint_Pad_D1.5mm, F.Cu at (209.7, 54.9)
- added TP429: TestPoint_Small, TestPoint:TestPoint_Pad_D1.5mm, F.Cu at (209.7, 58.4)
- added U104: TPS61287RZPR, Custom_Global_Footprints:RZP0014A-MFG, F.Cu at (203.5, 62.6)
- added U405: LM1085IS-12/NOPB, Package_TO_SOT_SMD:TO-263-3_TabPin2, F.Cu at (182.1, 29.6)
- added U406: LM1085IS-12/NOPB, Package_TO_SOT_SMD:TO-263-3_TabPin2, F.Cu at (182.1, 42.0)
- BT500: moved to F.Cu
- C404: value 47uF -> 330uF; footprint Capacitor_SMD:CP_Elec_6.3x5.8 -> Capacitor_Tantalum_SMD:CP_EIA-7343-31_Kemet-D
- C405: value 1uF -> 330uF; footprint Capacitor_SMD:C_0603_1608Metric -> Capacitor_Tantalum_SMD:CP_EIA-7343-31_Kemet-D
- C406: value 1uF -> 470uF; footprint Capacitor_SMD:C_0603_1608Metric -> Capacitor_Tantalum_SMD:CP_EIA-7360-38_Kemet-E
- C500: footprint Capacitor_SMD:C_0603_1608Metric -> Capacitor_SMD:C_0805_2012Metric
- C601, C603: footprint Custom_Global_Footprints:EEEFK1V470P -> Capacitor_SMD:CP_Elec_10x10
- D100, D101, D200, D300, D301, D302, D400, D403, D404, D405, D700, D701: footprint Custom_Global_Footprints:SML-P13PTT_LED_0402_1005Metric -> LED_SMD:LED_0402_1005Metric
- Q202: value DMP6050SSD -> DMP6050SSD-13
- Q203, Q301, Q500, Q702, Q703: value NVTA7002NT1G -> IRLML2402TRPBF; footprint Custom_Global_Footprints:NVTA7002N -> Package_TO_SOT_SMD:SOT-23
- Q300, Q700, Q701: value BSS314PE -> BSS314PEH6327
- TP402, TP403, TP405: footprint TestPoint:TestPoint_Pad_D1.0mm -> TestPoint:TestPoint_Pad_D1.5mm
- U101: value CP2102N-A02-GQFN24 -> CP2102N-A02-GQFN24R
- U403, U404: value XC6220B331MR -> XC6220B331MR-G
- U501: value ESP32-WROOM-32E -> ESP32-WROOM-32E-N4
- moved C206 153.8 mm to (112.7, 164.4), turned to 0 degrees
- moved C205 153.5 mm to (112.7, 162.4), turned to 0 degrees
- moved Q203 150.9 mm to (113.7, 159.2), turned to 0 degrees
- moved D200 149.3 mm to (115.8, 162.4), turned to 0 degrees
- moved R204 146.1 mm to (123.8, 159.4)
- moved R208 142.8 mm to (126.7, 159.4), turned to 0 degrees
- moved Q201 141.3 mm to (125.2, 150.0)
- moved R207 141.0 mm to (126.7, 157.4)
- moved R206 140.6 mm to (126.7, 155.4)
- moved R205 140.1 mm to (126.7, 153.4)
- moved C204 139.9 mm to (120.4, 153.9)
- moved C200 139.1 mm to (120.4, 143.8), turned to 0 degrees
- moved R107 138.3 mm to (147.8, 158.6), turned to 0 degrees
- moved C202 138.1 mm to (120.4, 148.9)
- moved Q200 136.8 mm to (125.2, 145.1)
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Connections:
- C404 pad 1: +12V_PUMP -> Net-(Q204-D)
- C405 pad 1: Net-(Q401-D) -> +12V
- C405 pad 2: Net-(Q400-G) -> GND
- C406 pad 1: Net-(Q401-D) -> +12V
- TP402 pad 1: Net-(Q401-D) -> +VDD
- TP403 pad 1: /DC_DC_REGULATORS/BOOST_IND -> +VBUS
- TP405 pad 1: Net-(U401-FB) -> /USB_C_TO_SERIAL/DTR_SERIAL
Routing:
- net Net-(J100-SHIELD): track 0.00 -> 21.3 mm
- net +VDD: track 0.00 -> 18.5 mm, vias 0 -> 3
- net /USB_C_TO_SERIAL/DTR_SERIAL: track 0.00 -> 13.6 mm
- net /USB_C_TO_SERIAL/RTS_SERIAL: track 0.00 -> 8.61 mm
- net GND: track 0.00 -> 8.37 mm, vias 0 -> 14
- net +VBUS: track 8.70 -> 14.9 mm, vias 0 -> 5
- net /USB_C_TO_SERIAL/SER_TX: track 0.00 -> 4.76 mm
- net /USB_C_TO_SERIAL/USB_CONN_D-: track 2.34 -> 7.01 mm, vias 0 -> 2
- net /USB_C_TO_SERIAL/RST: track 0.00 -> 4.42 mm
- net /USB_C_TO_SERIAL/SER_RX: track 0.00 -> 3.89 mm
- net /USB_C_TO_SERIAL/USB_CONN_D+: track 2.31 -> 5.92 mm
- net /USB_C_TO_SERIAL/VBUS_VDIV: track 0.00 -> 3.25 mm
- net /USB_C_TO_SERIAL/USB_D+: track 0.00 -> 2.96 mm
- net /USB_C_TO_SERIAL/USB_D-: track 0.00 -> 2.96 mm
- net Net-(Q401-D): track 2.30 -> 0.00 mm
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- added copper zone on F.Cu, net +VBUS
- added copper zone on F.Cu, net GND
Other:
- board size 137.2 x 78 mm -> 30 x 17.2 mm

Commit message: PCB desing in progresssss
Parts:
- moved TP415 65.2 mm to (178.2, 152.7)
- moved TP416 65.2 mm to (178.2, 156.3)
- moved TP417 65.2 mm to (181.7, 145.6)
- moved TP418 65.2 mm to (181.7, 149.2)
- moved TP413 65.0 mm to (178.0, 145.8)
- moved TP414 65.0 mm to (178.0, 149.4)
- moved TP419 65.0 mm to (181.5, 152.9)
- moved C105 36.0 mm to (111.9, 157.7)
- moved C106 36.0 mm to (111.9, 158.7)
- moved J100 36.0 mm to (112.5, 151.8)
- moved R107 36.0 mm to (111.9, 159.7)
- moved C104 36.0 mm to (119.8, 150.1)
- moved U100 36.0 mm to (120.2, 151.8)
- moved TP403 32.9 mm to (123.7, 151.6)
- moved Q203 22.6 mm to (133.3, 147.8), turned to 180 degrees
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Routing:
- net +VDDD: track 0.00 -> 28.6 mm, vias 0 -> 4
- net /USB_C_POWER_DELIVERY/VBUS_FET_EN: track 0.00 -> 13.1 mm
- net /BATTERY_MANAGEMENT_IC/VBUS_FET_SAFE_EN: track 0.00 -> 11.3 mm
- net Net-(Q202A-S1): track 0.00 -> 4.76 mm
- net /USB_C_POWER_DELIVERY/ISNK_FINE: track 0.00 -> 4.41 mm
- net Net-(Q200-S-Pad1): track 0.00 -> 4.29 mm
- net GND: track 8.37 -> 12.6 mm, vias 14 -> 26
- net /USB_C_POWER_DELIVERY/VBUS_MIN: track 0.00 -> 4.05 mm
- net /USB_C_POWER_DELIVERY/VBUS_MAX: track 0.00 -> 3.85 mm
- net /USB_C_POWER_DELIVERY/ISNK_COARSE: track 0.00 -> 3.79 mm
- net +VBUS: track 14.9 -> 18.5 mm
- net /USB_C_POWER_DELIVERY/FAULT: track 0.00 -> 2.46 mm
- net /USB_C_POWER_DELIVERY/VCCD: track 0.00 -> 2.15 mm
- net ESP_SCL: track 0.00 -> 1.72 mm
- net Net-(U200-FLIP): track 0.00 -> 1.42 mm
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- added copper zone on F.Cu, net +VDDD
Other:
- board size 30 x 17.2 mm -> 46.7 x 21.4 mm
